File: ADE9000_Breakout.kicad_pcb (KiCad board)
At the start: 2 copper layers, 57 parts, among them J1 PWR, J2 Current In, J3 Voltage In, Y1 24.576MHz

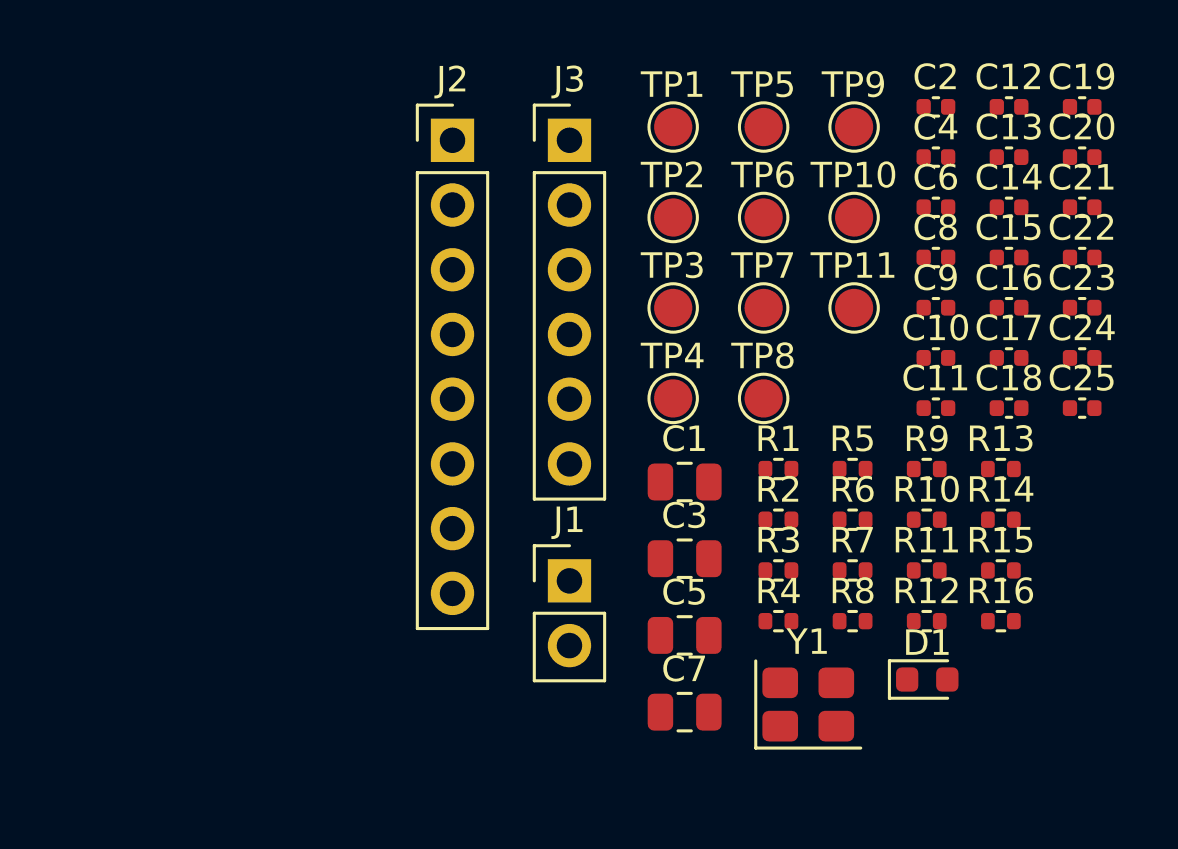
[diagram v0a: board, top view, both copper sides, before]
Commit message: Make PCB and design skills
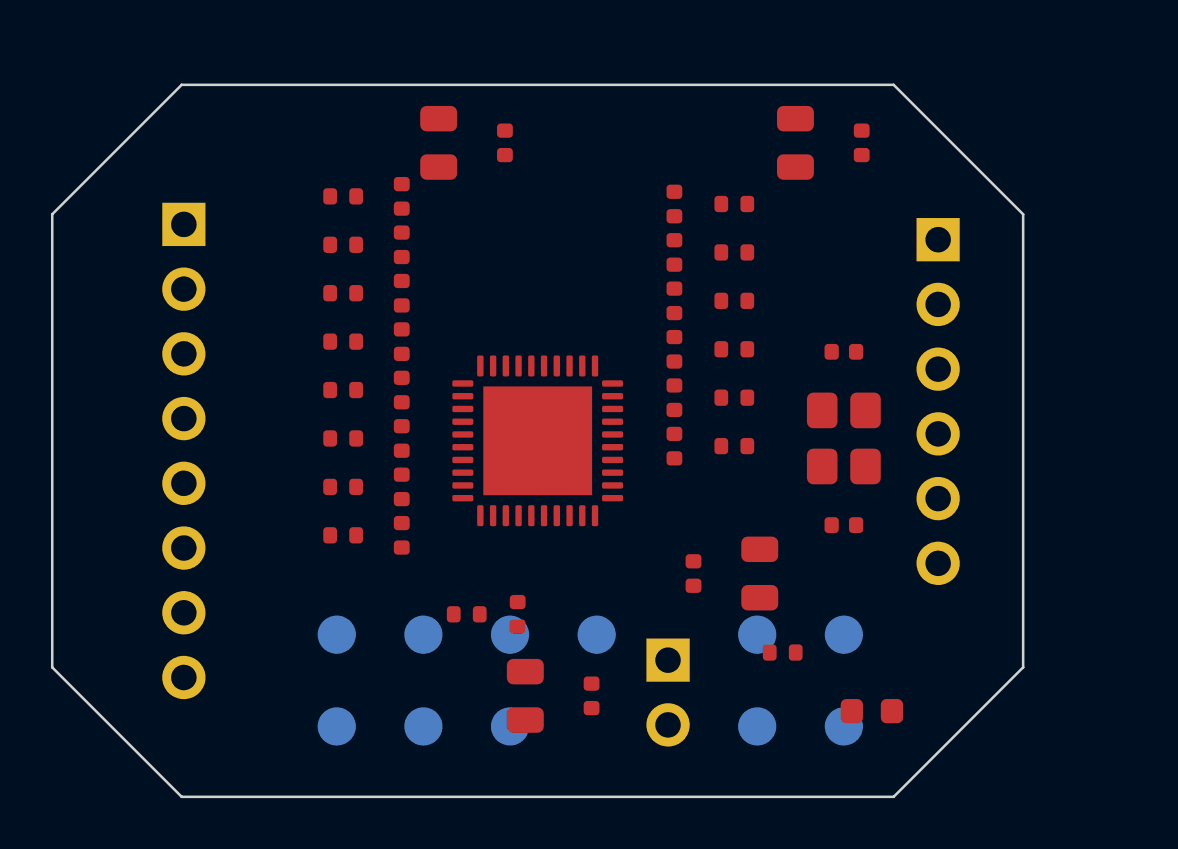
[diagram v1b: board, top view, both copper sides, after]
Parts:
- added U1: ADE9000, QFN-40-1EP_6x6mm_P0.5mm_EP4.6x4.6mm, F.Cu at (139.9, 96.4)
- TP1, TP10, TP11, TP2, TP3, TP4, TP5, TP6, TP7, TP8, TP9: moved to B.Cu
- moved C19 31.6 mm to (134.6, 100.1), turned to 90 degrees
- moved TP6 26.1 mm to (132.0, 107.6)
- moved C4 25.1 mm to (142.0, 106.4), turned to 90 degrees
- moved C12 24.1 mm to (134.6, 86.8), turned to 90 degrees
- moved C13 24.1 mm to (134.6, 88.7), turned to 90 degrees
- moved C14 24.1 mm to (134.6, 90.6), turned to 90 degrees
- moved C15 24.1 mm to (134.6, 92.5), turned to 90 degrees
- moved C16 24.1 mm to (134.6, 94.4), turned to 90 degrees
- moved C17 24.0 mm to (134.6, 96.3), turned to 90 degrees
- moved C18 24.0 mm to (134.6, 98.2), turned to 90 degrees
- moved TP11 24.0 mm to (132.0, 104.0)
- moved TP9 23.8 mm to (148.5, 107.6)
- moved R9 23.0 mm to (132.2, 100.1)
- moved C7 22.8 mm to (150.0, 84.7), turned to 90 degrees
- moved TP1 22.2 mm to (135.4, 104.0)
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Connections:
- net /+3V3 renamed +3V3
- net /AVDDOUT renamed AVDDOUT
- net /CF2 renamed CF2
- net /CF2_LED renamed CF2_LED
- net /CLKOUT renamed CLKOUT
- net /DVDDOUT renamed DVDDOUT
- net /IAN_J renamed IAN_J
- net /IAP renamed IAP
- net /IAP_J renamed IAP_J
- net /IBN_J renamed IBN_J
- net /IBP_J renamed IBP_J
- net /ICN_J renamed ICN_J
- net /ICP_J renamed ICP_J
- net /INN_J renamed INN_J
- net /INP_J renamed INP_J
- net /REF renamed REF
- net /RESET renamed RESET
- net /VAN_J renamed VAN_J
- net /VAP renamed VAP
- net /VAP_J renamed VAP_J
- net /VBN_J renamed VBN_J
- net /VBP_J renamed VBP_J
- net /VCN_J renamed VCN_J
- net /VCP_J renamed VCP_J
- C1 pad 1: /CLKIN -> GND
- C10 pad 1: /CLKIN -> CLKIN
- C11 pad 1: /CLKIN -> GND
- C12 pad 2: /CLKIN -> GND
- C13 pad 1: /CLKIN -> GND
- C13 pad 2: /CLKIN -> GND
- C14 pad 1: /CLKIN -> GND
- C14 pad 2: /CLKIN -> GND
- C15 pad 1: /CLKIN -> GND
- C15 pad 2: /CLKIN -> GND
- C16 pad 1: /CLKIN -> GND
- C16 pad 2: /CLKIN -> GND
- C17 pad 1: /CLKIN -> GND
- C17 pad 2: /CLKIN -> GND
- C18 pad 1: /CLKIN -> GND
- C18 pad 2: /CLKIN -> GND
- C19 pad 1: /CLKIN -> GND
- C19 pad 2: /CLKIN -> GND
- C2 pad 1: /CLKIN -> GND
- C20 pad 1: /CLKIN -> GND
- C20 pad 2: /CLKIN -> GND
- C21 pad 2: /CLKIN -> GND
- C22 pad 1: /CLKIN -> GND
- C22 pad 2: /CLKIN -> VCP
- C23 pad 1: /CLKIN -> GND
- C23 pad 2: /CLKIN -> GND
- C24 pad 1: /CLKIN -> GND
- C24 pad 2: /CLKIN -> GND
- C25 pad 1: /CLKIN -> VCP
- C25 pad 2: /CLKIN -> GND
- C3 pad 1: /CLKIN -> GND
- C4 pad 1: /CLKIN -> GND
- C5 pad 1: /CLKIN -> GND
- C6 pad 1: /CLKIN -> GND
- C7 pad 1: /CLKIN -> GND
- C8 pad 1: /CLKIN -> GND
- C9 pad 1: /CLKIN -> GND
- C9 pad 2: unconnected-(C9-Pad2) -> CLKIN
- D1 pad 1: /CLKIN -> GND
- J1 pad 2: /CLKIN -> GND
- R10 pad 2: /CLKIN -> GND
- R12 pad 2: /CLKIN -> GND
- R13 pad 2: /CLKIN -> GND
- R14 pad 2: /CLKIN -> GND
- R15 pad 2: /CLKIN -> VCP
- R3 pad 2: /CLKIN -> GND
- R4 pad 2: /CLKIN -> GND
- R5 pad 2: /CLKIN -> GND
- R6 pad 2: /CLKIN -> GND
- R7 pad 2: /CLKIN -> GND
- R8 pad 2: /CLKIN -> GND
- R9 pad 2: /CLKIN -> GND
- TP1 pad 1: /SS -> SS
- TP10 pad 1: /CF4_DREADY -> CF4_DREADY
- TP2 pad 1: /MOSI -> MOSI
- TP3 pad 1: /MISO -> MISO
- TP4 pad 1: /SCLK -> SCLK
- TP5 pad 1: /IRQ0 -> IRQ0
- TP6 pad 1: /IRQ1 -> IRQ1
- TP7 pad 1: /CF1 -> CF1
- TP9 pad 1: /CF3_ZX -> CF3_ZX
- Y1 pad 1: /CLKIN -> CLKIN
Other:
- board outline added: 38.1 x 27.9 mm

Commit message: Complete routing
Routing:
- net GND: track 0.00 -> 134.6 mm
- net CF4_DREADY: track 0.00 -> 41.0 mm, vias 0 -> 1
- net +3V3: track 0.00 -> 39.0 mm, vias 0 -> 4
- net CF2: track 0.00 -> 37.1 mm, vias 0 -> 2
- net SCLK: track 0.00 -> 36.9 mm, vias 0 -> 1
- net CF3_ZX: track 0.00 -> 32.2 mm, vias 0 -> 1
- net IRQ1: track 0.00 -> 28.4 mm, vias 0 -> 1
- net CLKIN: track 0.00 -> 27.3 mm, vias 0 -> 2
- net REF: track 0.00 -> 26.5 mm, vias 0 -> 2
- net CF1: track 0.00 -> 23.6 mm, vias 0 -> 1
- net CLKOUT: track 0.00 -> 23.0 mm, vias 0 -> 2
- net VCP: track 0.00 -> 19.4 mm, vias 0 -> 2
- net RESET: track 0.00 -> 16.5 mm, vias 0 -> 2
- net DVDDOUT: track 0.00 -> 16.3 mm
- net VAP: track 0.00 -> 16.2 mm, vias 0 -> 2
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
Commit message: Some silk screen vagaries
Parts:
- added H1: MountingHole_2.2mm_M2, MountingHole:MountingHole_2.2mm_M2, F.Cu at (124.2, 85.0)
- added H2: MountingHole_2.2mm_M2, MountingHole:MountingHole_2.2mm_M2, F.Cu at (155.5, 85.0)
- added H3: MountingHole_2.2mm_M2, MountingHole:MountingHole_2.2mm_M2, F.Cu at (124.2, 108.7)
- added H4: MountingHole_2.2mm_M2, MountingHole:MountingHole_2.2mm_M2, F.Cu at (155.8, 108.5)
- added LOGO1: OSHW-LOGOM, Symbol:OSHW-Logo2_7.3x6mm_SilkScreen, B.Cu at (139.8, 90.3)
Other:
- board text added: "ADE9000 Breakout"
- board text added: "by Tisham Dhar https://whatnick.com v0.1 09/05/2026"

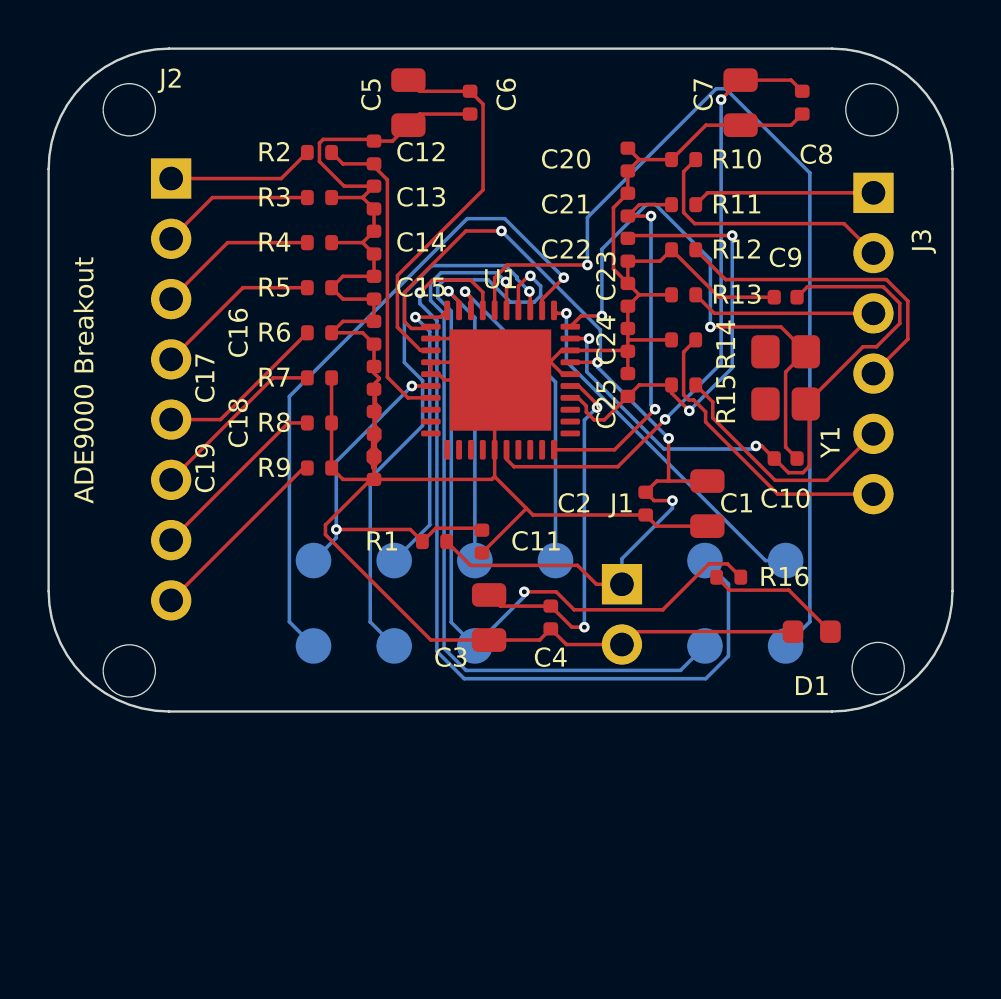
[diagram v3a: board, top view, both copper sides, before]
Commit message: Reroute with JST connector for SPI
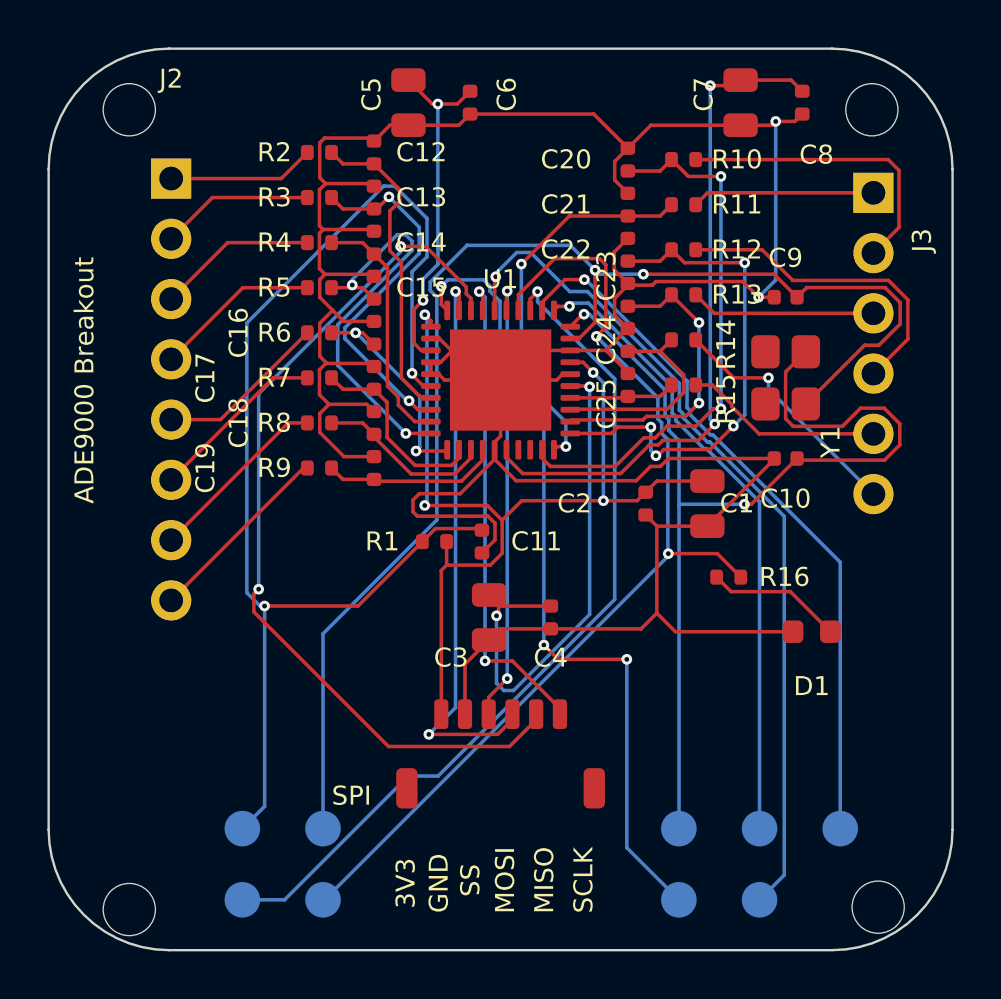
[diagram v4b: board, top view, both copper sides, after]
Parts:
- removed TP3: MISO, TestPoint:TestPoint_Pad_D1.5mm
- removed TP4: SCLK, TestPoint:TestPoint_Pad_D1.5mm
- J1: value PWR -> SPI JST-SH; footprint Connector_PinHeader_2.54mm:PinHeader_1x02_P2.54mm_Vertical -> JST_SHL_SM06B-SHLS-TF_1x06-1MP_P1.00mm_Horizontal
- TP12: renamed from TP1; value SS -> CLKIN
- TP13: renamed from TP2; value MOSI -> CLKOUT
- moved TP6 23.5 mm to (154.2, 115.3)
- moved TP13 14.2 mm to (147.4, 115.3)
- moved TP7 12.5 mm to (129.0, 118.3)
- moved TP8 12.5 mm to (132.4, 118.3)
- moved TP11 11.7 mm to (129.0, 115.3)
- moved TP12 11.7 mm to (132.4, 115.3)
- moved TP5 11.4 mm to (150.8, 115.3)
- moved TP10 10.8 mm to (150.8, 118.3)
- moved TP9 10.8 mm to (147.4, 118.3)
- moved H4 10.1 mm to (155.8, 118.6)
- moved H3 10.1 mm to (124.2, 118.7)
- moved J1 8.79 mm to (139.9, 112.2)
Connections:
- C10 pad 1: CLKIN -> GND
- C13 pad 1: GND -> IAN
- C14 pad 1: GND -> IBP
- C15 pad 1: GND -> IBN
- C16 pad 1: GND -> ICP
- C17 pad 1: GND -> ICN
- C18 pad 1: GND -> INP
- C19 pad 1: GND -> INN
- C20 pad 1: GND -> VAN
- C22 pad 1: GND -> VBN
- C22 pad 2: VCP -> GND
- C23 pad 1: GND -> VBP
- C24 pad 1: GND -> VCN
- R10 pad 2: GND -> VAN
- R12 pad 2: GND -> VBN
- R13 pad 2: GND -> VBP
- R14 pad 2: GND -> VCN
- R3 pad 2: GND -> IAN
- R4 pad 2: GND -> IBP
- R5 pad 2: GND -> IBN
- R6 pad 2: GND -> ICP
- R7 pad 2: GND -> ICN
- R8 pad 2: GND -> INP
- R9 pad 2: GND -> INN
- TP12 pad 1: SS -> CLKIN
- TP13 pad 1: MOSI -> CLKOUT
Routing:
- net RESET: track 16.5 -> 51.1 mm
- net CLKIN: track 27.3 -> 56.7 mm
- net MISO: track 13.8 -> 37.5 mm, vias 1 -> 2
- net VAN: track 0.00 -> 23.2 mm, vias 0 -> 2
- net CLKOUT: track 23.0 -> 44.3 mm
- net VBN: track 0.00 -> 21.0 mm, vias 0 -> 4
- net IBN: track 0.00 -> 17.4 mm, vias 0 -> 2
- net SCLK: track 36.9 -> 20.8 mm, vias 1 -> 2
- net IAN: track 0.00 -> 15.5 mm, vias 0 -> 2
- net VCP: track 19.4 -> 4.49 mm, vias 2 -> 0
- net VBP: track 0.00 -> 12.8 mm, vias 0 -> 2
- net CF1: track 23.6 -> 36.2 mm
- net IRQ0: track 15.3 -> 26.8 mm
- net MOSI: track 12.8 -> 24.0 mm, vias 1 -> 2
- net IBP: track 0.00 -> 10.4 mm
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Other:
- board size 38.1 x 27.9 mm -> 38.1 x 38 mm
- board text added: "3V3"
- board text added: "CF1"
- board text added: "CF2"
- board text added: "CF3/ZX"
- board text added: "CLKIN"
- board text added: "CLKOUT"
- board text added: "DRDY"
- board text added: "GND"
- board text added: "IRQ0"
- board text added: "IRQ1"
- board text added: "MISO"
- board text added: "MOSI"
- board text added: "RESET"
- board text added: "SCLK"
- board text added: "SPI"
- board text added: "SS"

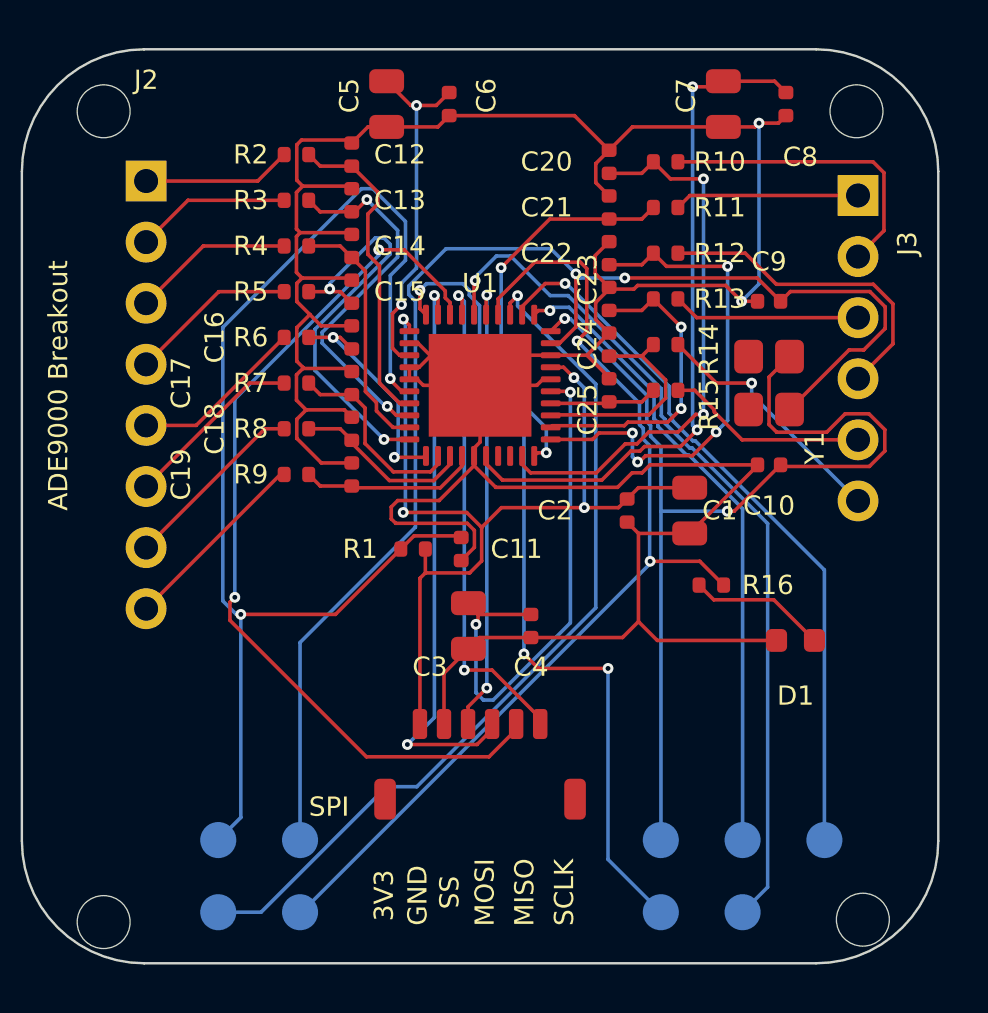
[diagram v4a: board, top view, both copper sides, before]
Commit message: Move decoupling closer
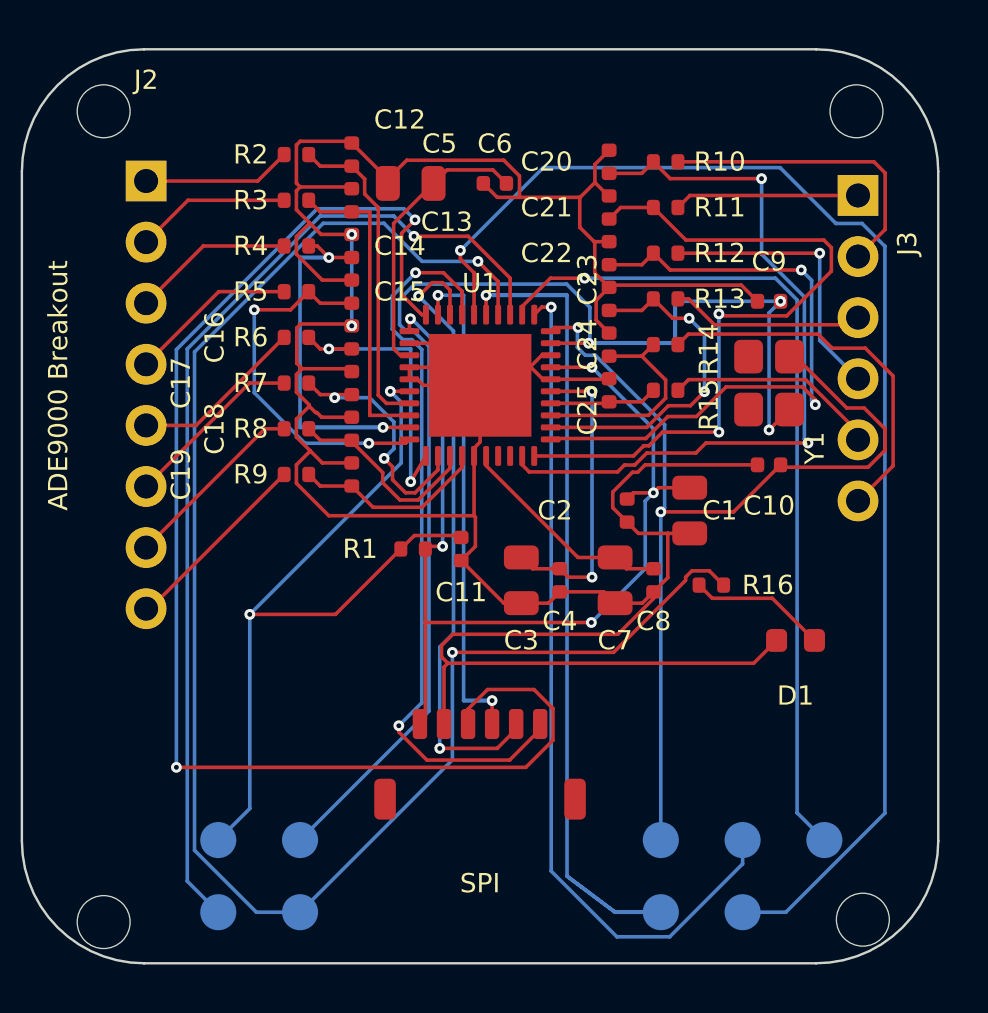
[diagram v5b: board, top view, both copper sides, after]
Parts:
- moved C8 20.5 mm to (147.1, 104.5)
- moved C7 20.3 mm to (145.5, 104.5)
- moved C6 3.81 mm to (140.5, 88.0), turned to 0 degrees
- moved C5 3.45 mm to (137.0, 88.0), turned to 0 degrees
- moved C3 2.91 mm to (141.6, 104.5)
- moved C4 2.25 mm to (143.2, 104.5)
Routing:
- net SS: track 22.1 -> 56.9 mm
- net CF2: track 42.8 -> 69.8 mm
- net REF: track 28.8 -> 9.14 mm, vias 2 -> 0
- net CF4_DREADY: track 36.1 -> 54.5 mm
- net RESET: track 51.1 -> 33.0 mm
- net VAP: track 16.4 -> 29.6 mm
- net MISO: track 37.5 -> 26.1 mm
- net SCLK: track 20.8 -> 31.0 mm
- net CF3_ZX: track 31.2 -> 40.5 mm, vias 3 -> 1
- net AVDDOUT: track 21.9 -> 12.7 mm
- net IBP: track 10.4 -> 19.4 mm, vias 0 -> 2
- net IRQ0: track 26.8 -> 35.6 mm
- net VAN: track 23.2 -> 31.5 mm
- net CF1: track 36.2 -> 42.3 mm
- net VBN: track 21.0 -> 26.7 mm, vias 4 -> 2
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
